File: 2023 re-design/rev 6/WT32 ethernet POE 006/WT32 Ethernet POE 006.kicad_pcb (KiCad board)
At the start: 4 copper layers, 42 x 38 mm, 52 parts, among them J1 Ethernet, U1 AP63205WU, U2 W5500, U3 LM1117-3.3, Y1 25MHz_SMD_Crystal_Resonator

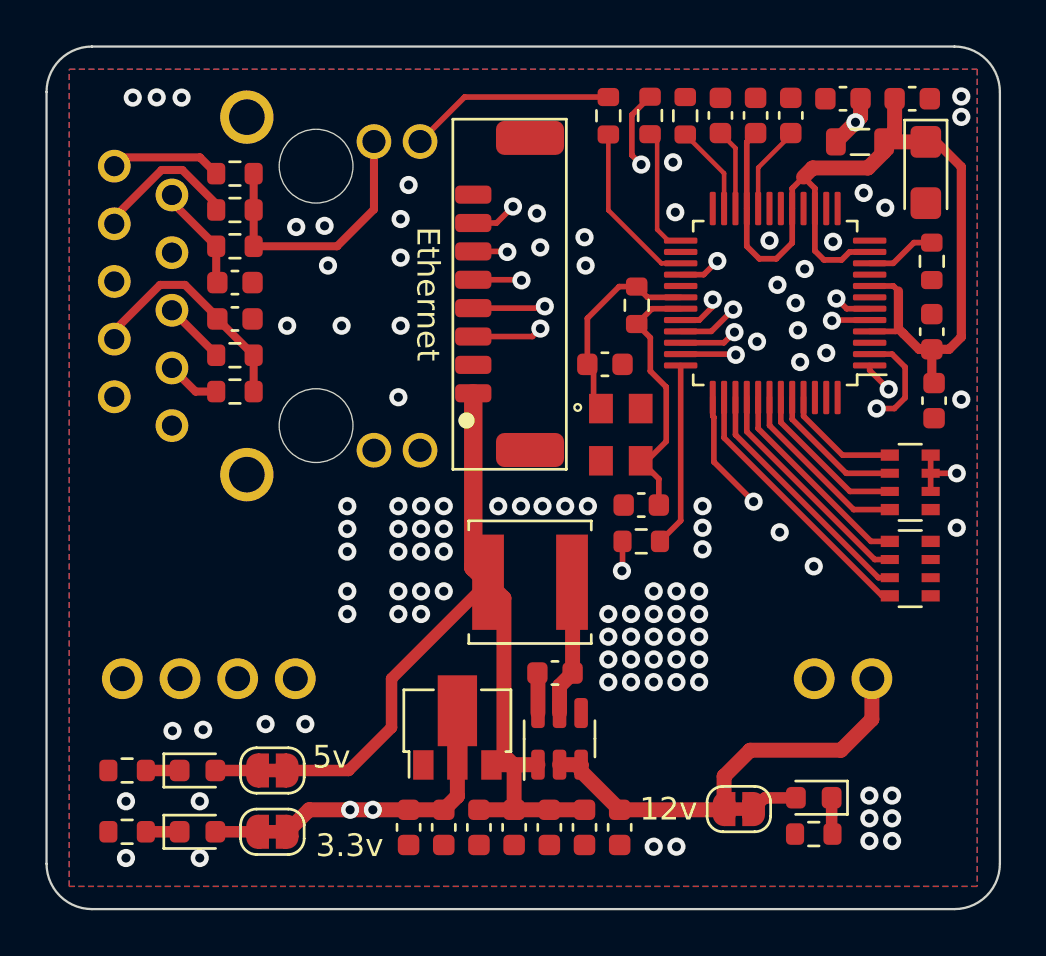
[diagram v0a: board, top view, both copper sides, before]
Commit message: nudged the large inductor
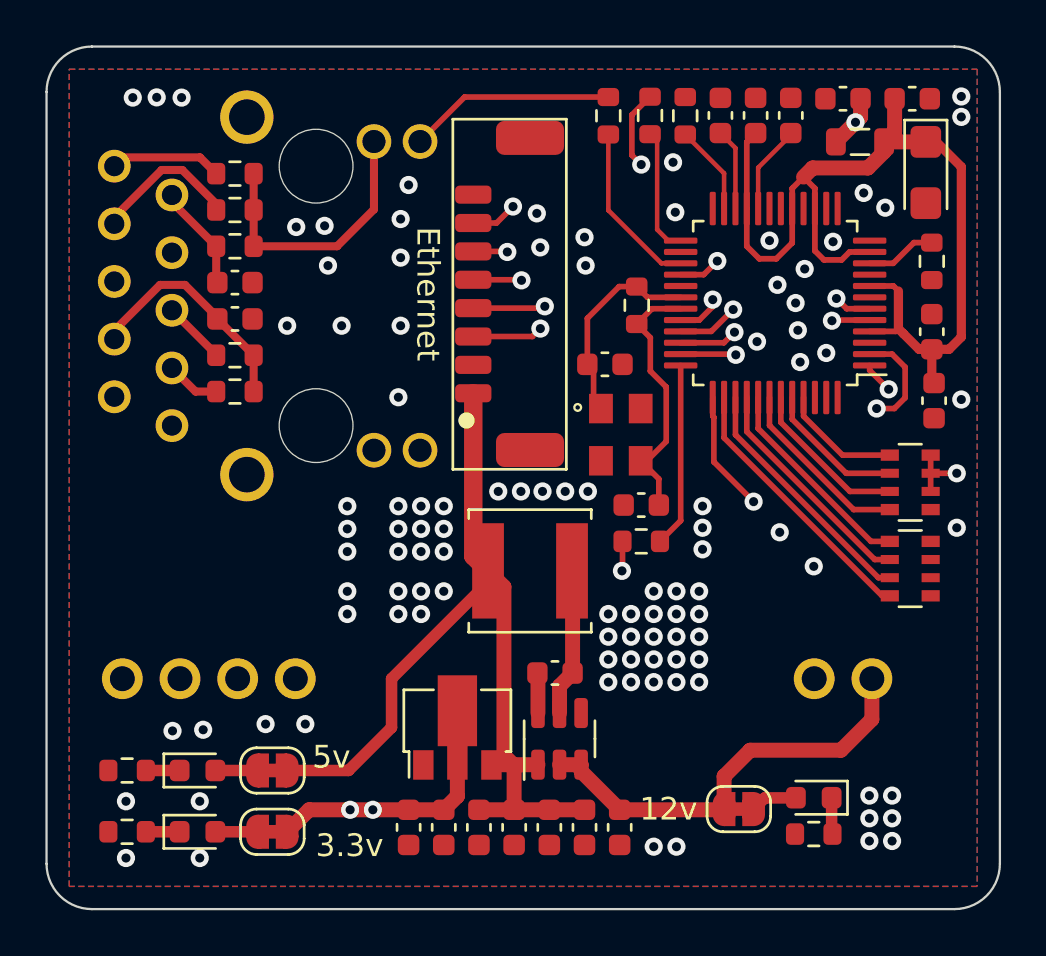
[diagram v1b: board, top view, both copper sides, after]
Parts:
- moved L2 0.50 mm to (41.3, 43.1)
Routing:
- net Net-(C5-Pad1): track 6.01 -> 7.01 mm
- net +5V: track 39.4 -> 39.9 mm

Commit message: update inductor footprint
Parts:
- moved L2 0.60 mm to (40.7, 43.1)
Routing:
- net GND: vias 102 -> 126
